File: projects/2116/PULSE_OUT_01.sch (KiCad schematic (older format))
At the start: 52 parts, among them CN4 HIF3FC-16PA-2.54DS, CN5 HIF3FC-16PA-2.54DS, CN6 HIF3FC-16PA-2.54DSA, CN7 HIF3FC-16PA-2.54DSA, IC24 74HCT574, IC25 74HCT574, IC26 74HCT574, IC27 74HCT574, IC28 74HCT541, IC29 74HCT541, IC30 74HCT541, IC31 74HCT541

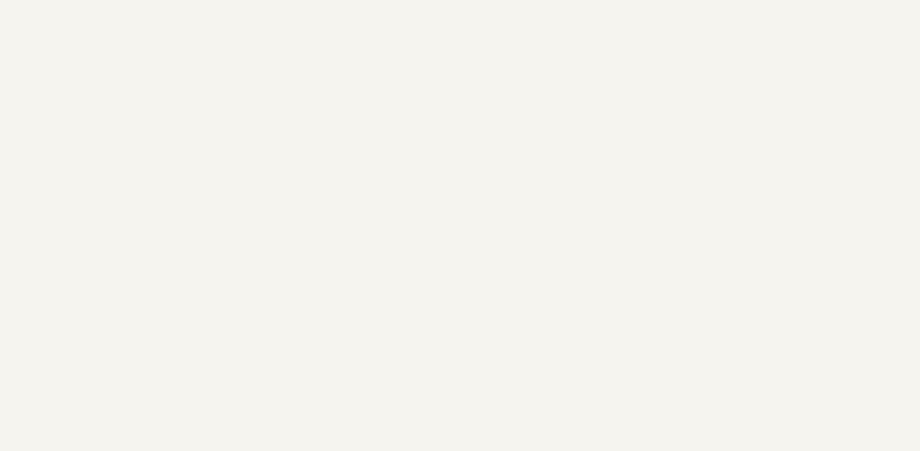
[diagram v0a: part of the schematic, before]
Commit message: 基板端に電源コネクタを追加。
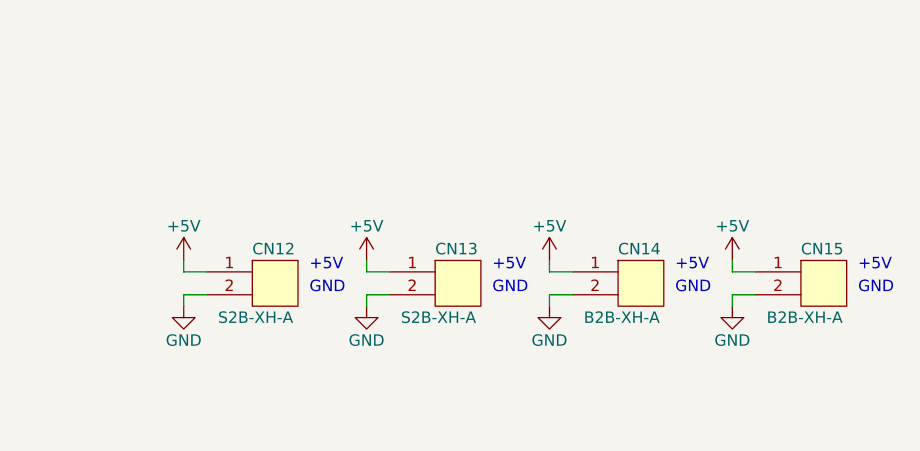
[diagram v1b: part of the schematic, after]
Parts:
- added CN12, CN13: S2B-XH-A, A01myFootPrint:S2B-XH-A, symbol connectors:2PIN
- added CN14, CN15: B2B-XH-A, A01myFootPrint:cn_B2B-XH-A, symbol connectors:2PIN
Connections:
- wire segments 324 -> 340
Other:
- note added: "+5V"
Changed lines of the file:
@@
 Wire Wire Line
 	3450 6550 3450 6600
+$Comp
+L connectors:2PIN CN12
+U 1 1 61B35381
+P 7400 6150
+F 0 "CN12" H 7300 6300 50  0000 L CNN
+F 1 "S2B-XH-A" H 7150 6000 50  0000 L CNN
+F 2 "A01myFootPrint:S2B-XH-A" H 7400 6150 60  0001 C CNN
+F 3 "" H 7400 6150 60  0001 C CNN
+	1    7400 6150
+	1    0    0    -1
+$EndComp
+$Comp
+L power:GND #PWR?
+U 1 1 61B364AA
+P 7000 6250
+AR Path="/61B364AA" Ref="#PWR?"  Part="1"
+AR Path="/61BC7329/61B364AA" Ref="#PWR?"  Part="1"
+AR Path="/61AA6AFE/61B364AA" Ref="#PWR0208"  Part="1"
+F 0 "#PWR0208" H 7000 6000 50  0001 C CNN
+F 1 "GND" H 7000 6100 50  0000 C CNN
+F 2 "" H 7000 6250 50  0001 C CNN
+F 3 "" H 7000 6250 50  0001 C CNN
+	1    7000 6250
+	1    0    0    -1
+$EndComp
+$Comp
+L power:+5V #PWR?
+U 1 1 61B36864
+P 7000 6050
+AR Path="/61B36864" Ref="#PWR?"  Part="1"
+AR Path="/61BC7329/61B36864" Ref="#PWR?"  Part="1"
+AR Path="/61AA6AFE/61B36864" Ref="#PWR0207"  Part="1"
+F 0 "#PWR0207" H 7000 5900 50  0001 C CNN
+F 1 "+5V" H 7000 6200 50  0000 C CNN
+F 2 "" H 7000 6050 50  0001 C CNN
+F 3 "" H 7000 6050 50  0001 C CNN
+	1    7000 6050
+	1    0    0    -1
+$EndComp
+Wire Wire Line
+	7100 6100 7000 6100
+Wire Wire Line
+	7000 6100 7000 6050
+Wire Wire Line
+	7100 6200 7000 6200
+Wire Wire Line
+	7000 6200 7000 6250
+Text Notes 7550 6200 0    50   ~ 0
+GND
+Text Notes 7550 6100 0    50   ~ 0
++5V
+$Comp
+L connectors:2PIN CN13
+U 1 1 61BD1111
+P 8200 6150
+F 0 "CN13" H 8100 6300 50  0000 L CNN
+F 1 "S2B-XH-A" H 7950 6000 50  0000 L CNN
+F 2 "A01myFootPrint:S2B-XH-A" H 8200 6150 60  0001 C CNN
+F 3 "" H 8200 6150 60  0001 C CNN
+	1    8200 6150
+	1    0    0    -1
+$EndComp
+$Comp
+L power:GND #PWR?
+U 1 1 61BD1117
+P 7800 6250
+AR Path="/61BD1117" Ref="#PWR?"  Part="1"
+AR Path="/61BC7329/61BD1117" Ref="#PWR?"  Part="1"
+AR Path="/61AA6AFE/61BD1117" Ref="#PWR0210"  Part="1"
+F 0 "#PWR0210" H 7800 6000 50  0001 C CNN
+F 1 "GND" H 7800 6100 50  0000 C CNN
+F 2 "" H 7800 6250 50  0001 C CNN
+F 3 "" H 7800 6250 50  0001 C CNN
+	1    7800 6250
+	1    0    0    -1
+$EndComp
+$Comp
+L power:+5V #PWR?
+U 1 1 61BD111D
+P 7800 6050
+AR Path="/61BD111D" Ref="#PWR?"  Part="1"
+AR Path="/61BC7329/61BD111D" Ref="#PWR?"  Part="1"
+AR Path="/61AA6AFE/61BD111D" Ref="#PWR0209"  Part="1"
+F 0 "#PWR0209" H 7800 5900 50  0001 C CNN
+F 1 "+5V" H 7800 6200 50  0000 C CNN
+F 2 "" H 7800 6050 50  0001 C CNN
+F 3 "" H 7800 6050 50  0001 C CNN
+	1    7800 6050
+	1    0    0    -1
+$EndComp
+Wire Wire Line
+	7900 6100 7800 6100
+Wire Wire Line
+	7800 6100 7800 6050
+Wire Wire Line
+	7900 6200 7800 6200
+Wire Wire Line
+	7800 6200 7800 6250
+Text Notes 8350 6200 0    50   ~ 0
+GND
+Text Notes 8350 6100 0    50   ~ 0
++5V
+$Comp
+L connectors:2PIN CN14
+U 1 1 61C04591
+P 9000 6150
+F 0 "CN14" H 8900 6300 50  0000 L CNN
+F 1 "B2B-XH-A" H 8750 6000 50  0000 L CNN
+F 2 "A01myFootPrint:cn_B2B-XH-A" H 9000 6150 60  0001 C CNN
+F 3 "" H 9000 6150 60  0001 C CNN
+	1    9000 6150
+	1    0    0    -1
+$EndComp
+$Comp
+L power:GND #PWR?
+U 1 1 61C04597
+P 8600 6250
+AR Path="/61C04597" Ref="#PWR?"  Part="1"
+AR Path="/61BC7329/61C04597" Ref="#PWR?"  Part="1"
+AR Path="/61AA6AFE/61C04597" Ref="#PWR0212"  Part="1"
+F 0 "#PWR0212" H 8600 6000 50  0001 C CNN
+F 1 "GND" H 8600 6100 50  0000 C CNN
+F 2 "" H 8600 6250 50  0001 C CNN
+F 3 "" H 8600 6250 50  0001 C CNN
+	1    8600 6250
+	1    0    0    -1
+$EndComp
+$Comp
+L power:+5V #PWR?
+U 1 1 61C0459D
+P 8600 6050
+AR Path="/61C0459D" Ref="#PWR?"  Part="1"
+AR Path="/61BC7329/61C0459D" Ref="#PWR?"  Part="1"
+AR Path="/61AA6AFE/61C0459D" Ref="#PWR0211"  Part="1"
+F 0 "#PWR0211" H 8600 5900 50  0001 C CNN
+F 1 "+5V" H 8600 6200 50  0000 C CNN
+F 2 "" H 8600 6050 50  0001 C CNN
+F 3 "" H 8600 6050 50  0001 C CNN
+	1    8600 6050
+	1    0    0    -1
+$EndComp
+Wire Wire Line
+	8700 6100 8600 6100
+Wire Wire Line
+	8600 6100 8600 6050
+Wire Wire Line
+	8700 6200 8600 6200
+Wire Wire Line
+	8600 6200 8600 6250
+Text Notes 9150 6200 0    50   ~ 0
+GND
+Text Notes 9150 6100 0    50   ~ 0
++5V
+$Comp
+L connectors:2PIN CN15
+U 1 1 61C387D0
+P 9800 6150
+F 0 "CN15" H 9700 6300 50  0000 L CNN
+F 1 "B2B-XH-A" H 9550 6000 50  0000 L CNN
+F 2 "A01myFootPrint:cn_B2B-XH-A" H 9800 6150 60  0001 C CNN
+F 3 "" H 9800 6150 60  0001 C CNN
+	1    9800 6150
+	1    0    0    -1
+$EndComp
+$Comp
+L power:GND #PWR?
+U 1 1 61C387D6
+P 9400 6250
+AR Path="/61C387D6" Ref="#PWR?"  Part="1"
+AR Path="/61BC7329/61C387D6" Ref="#PWR?"  Part="1"
+AR Path="/61AA6AFE/61C387D6" Ref="#PWR0214"  Part="1"
+F 0 "#PWR0214" H 9400 6000 50  0001 C CNN
+F 1 "GND" H 9400 6100 50  0000 C CNN
+F 2 "" H 9400 6250 50  0001 C CNN
+F 3 "" H 9400 6250 50  0001 C CNN
+	1    9400 6250
+	1    0    0    -1
+$EndComp
+$Comp
+L power:+5V #PWR?
+U 1 1 61C387DC
+P 9400 6050
+AR Path="/61C387DC" Ref="#PWR?"  Part="1"
+AR Path="/61BC7329/61C387DC" Ref="#PWR?"  Part="1"
+AR Path="/61AA6AFE/61C387DC" Ref="#PWR0213"  Part="1"
+F 0 "#PWR0213" H 9400 5900 50  0001 C CNN
+F 1 "+5V" H 9400 6200 50  0000 C CNN
+F 2 "" H 9400 6050 50  0001 C CNN
+F 3 "" H 9400 6050 50  0001 C CNN
+	1    9400 6050
+	1    0    0    -1
+$EndComp
+Wire Wire Line
+	9500 6100 9400 6100
+Wire Wire Line
+	9400 6100 9400 6050
+Wire Wire Line
+	9500 6200 9400 6200
+Wire Wire Line
+	9400 6200 9400 6250
+Text Notes 9950 6200 0    50   ~ 0
+GND
+Text Notes 9950 6100 0    50   ~ 0
++5V
 $EndSCHEMATC
